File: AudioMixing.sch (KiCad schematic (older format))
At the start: 38 parts, among them U6 MAX98089ETN+, Y2 830208220101

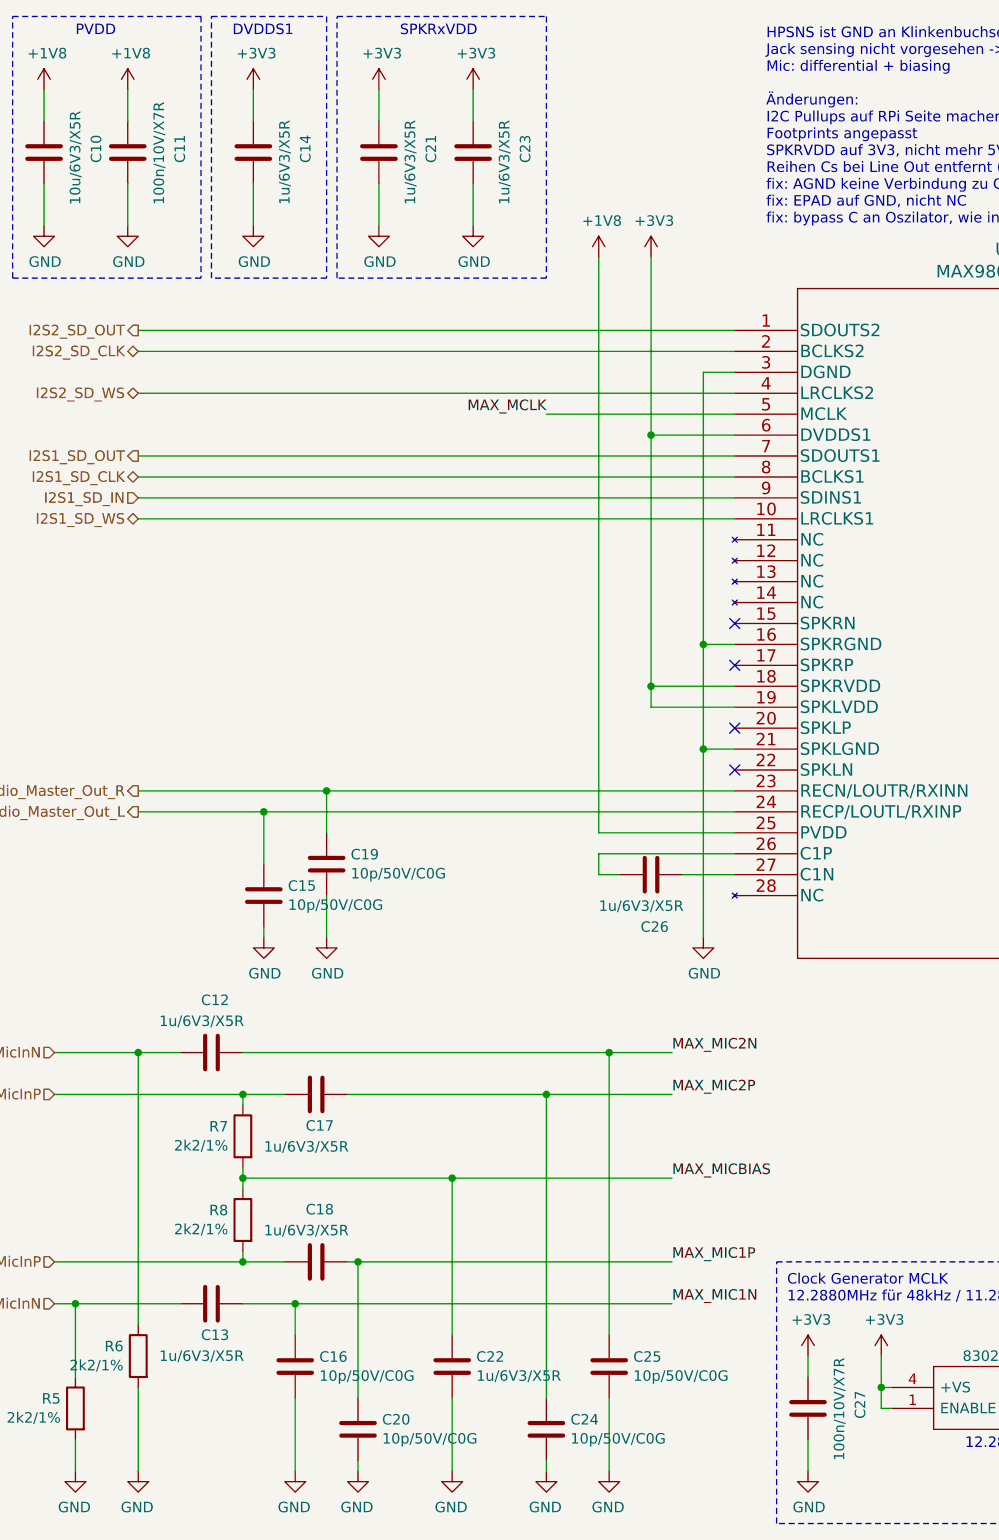
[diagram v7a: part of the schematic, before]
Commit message: - Platzoptimierungen
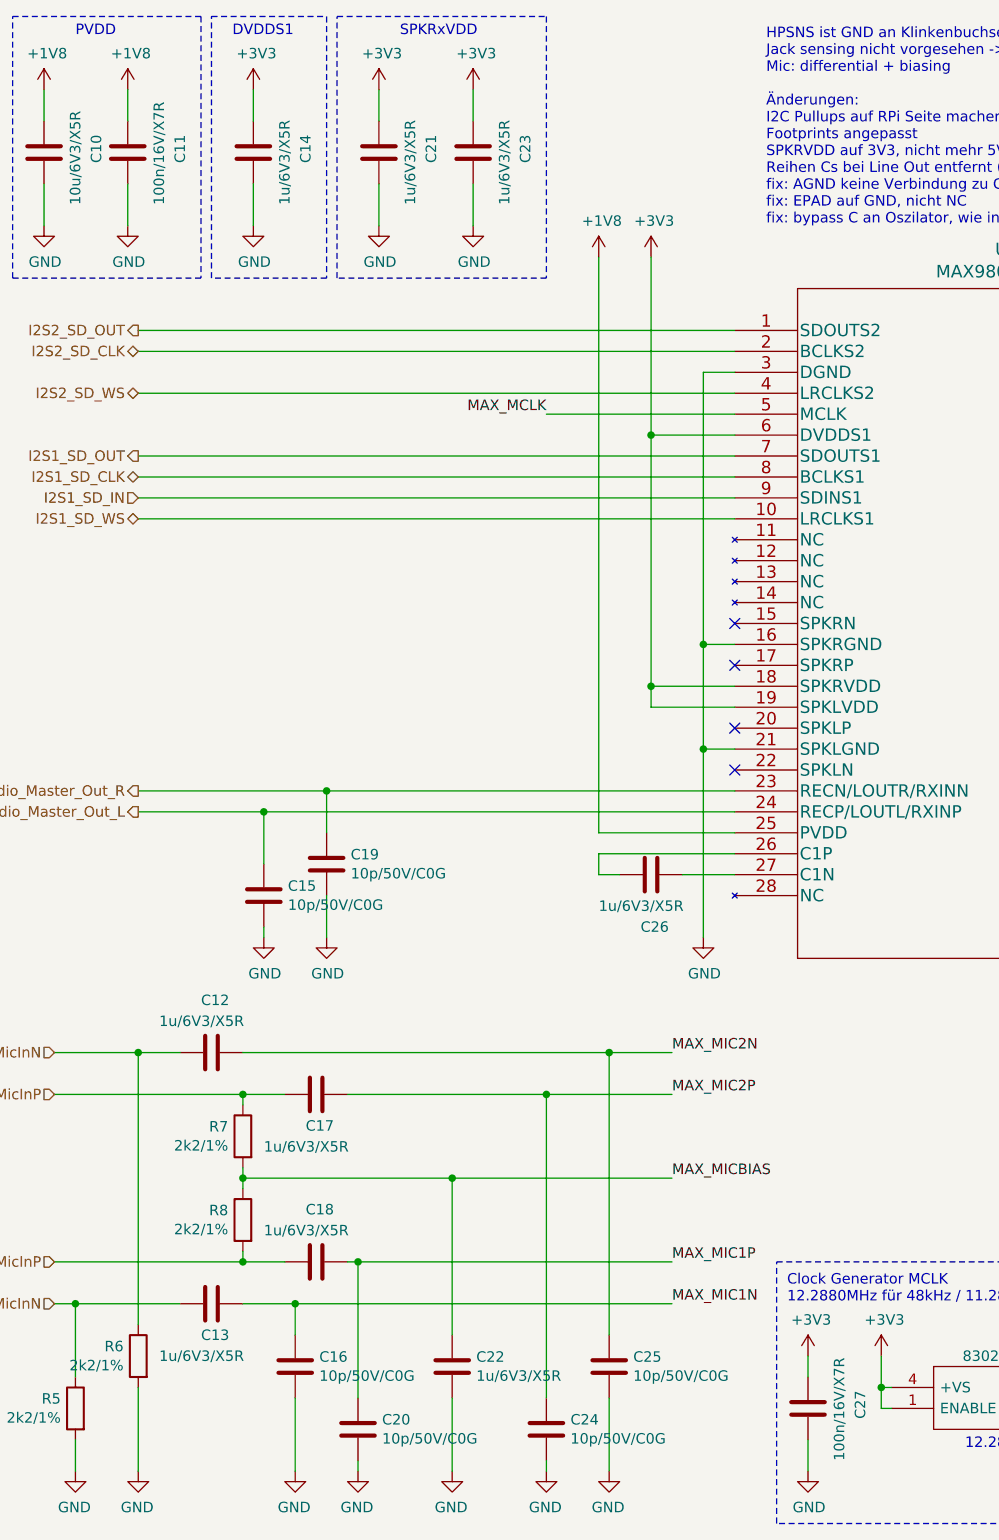
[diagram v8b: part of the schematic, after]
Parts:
- C10, C33: footprint Resistor_SMD:R_0603_1608Metric -> Capacitor_SMD:C_0603_1608Metric
- C11, C27: value 100n/10V/X7R -> 100n/16V/X7R; footprint Resistor_SMD:R_0603_1608Metric -> Capacitor_SMD:C_0402_1005Metric
- C12, C13, C14, C15, C16, C17, C18, C19, C20, C21, C22, C23, C24, C25, C26, C28, C29, C30, C31, C32, C34, C35, C36, C37, C38, C39, C40: footprint Resistor_SMD:R_0603_1608Metric -> Capacitor_SMD:C_0402_1005Metric
- R5, R6, R7, R8, R9: footprint Resistor_SMD:R_0603_1608Metric -> Resistor_SMD:R_0402_1005Metric
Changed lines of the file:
@@
 F 0 "C15" H 2415 4796 50  0000 L CNN
 F 1 "10p/50V/C0G" H 2415 4705 50  0000 L CNN
-F 2 "Resistor_SMD:R_0603_1608Metric" H 2338 4600 50  0001 C CNN
+F 2 "Capacitor_SMD:C_0402_1005Metric" H 2338 4600 50  0001 C CNN
 F 3 "~" H 2300 4750 50  0001 C CNN
 	1    2300 4750
@@
 F 0 "C19" H 2715 4646 50  0000 L CNN
 F 1 "10p/50V/C0G" H 2715 4555 50  0000 L CNN
-F 2 "Resistor_SMD:R_0603_1608Metric" H 2638 4450 50  0001 C CNN
+F 2 "Capacitor_SMD:C_0402_1005Metric" H 2638 4450 50  0001 C CNN
 F 3 "~" H 2600 4600 50  0001 C CNN
 	1    2600 4600
@@
 F 0 "C30" H 8165 5346 50  0000 L CNN
 F 1 "10p/50V/C0G" H 8165 5255 50  0000 L CNN
-F 2 "Resistor_SMD:R_0603_1608Metric" H 8088 5150 50  0001 C CNN
+F 2 "Capacitor_SMD:C_0402_1005Metric" H 8088 5150 50  0001 C CNN
 F 3 "~" H 8050 5300 50  0001 C CNN
 	1    8050 5300
@@
 F 0 "C31" H 8465 4946 50  0000 L CNN
 F 1 "10p/50V/C0G" H 8465 4855 50  0000 L CNN
-F 2 "Resistor_SMD:R_0603_1608Metric" H 8388 4750 50  0001 C CNN
+F 2 "Capacitor_SMD:C_0402_1005Metric" H 8388 4750 50  0001 C CNN
 F 3 "~" H 8350 4900 50  0001 C CNN
 	1    8350 4900
@@
 F 0 "C36" H 9515 4946 50  0000 L CNN
 F 1 "10p/50V/C0G" H 9515 4855 50  0000 L CNN
-F 2 "Resistor_SMD:R_0603_1608Metric" H 9438 4750 50  0001 C CNN
+F 2 "Capacitor_SMD:C_0402_1005Metric" H 9438 4750 50  0001 C CNN
 F 3 "~" H 9400 4900 50  0001 C CNN
 	1    9400 4900
@@
 F 0 "C39" H 9865 5146 50  0000 L CNN
 F 1 "10p/50V/C0G" H 9865 5055 50  0000 L CNN
-F 2 "Resistor_SMD:R_0603_1608Metric" H 9788 4950 50  0001 C CNN
+F 2 "Capacitor_SMD:C_0402_1005Metric" H 9788 4950 50  0001 C CNN
 F 3 "~" H 9750 5100 50  0001 C CNN
 	1    9750 5100
@@
 F 0 "C26" V 4400 4600 50  0000 L CNN
 F 1 "1u/6V3/X5R" V 4300 4400 50  0000 L CNN
-F 2 "Resistor_SMD:R_0603_1608Metric" H 4188 4500 50  0001 C CNN
+F 2 "Capacitor_SMD:C_0402_1005Metric" H 4188 4500 50  0001 C CNN
 F 3 "~" H 4150 4650 50  0001 C CNN
 	1    4150 4650
@@
 F 0 "C29" H 7865 5146 50  0000 L CNN
 F 1 "1u/6V3/X5R" H 7865 5055 50  0000 L CNN
-F 2 "Resistor_SMD:R_0603_1608Metric" H 7788 4950 50  0001 C CNN
+F 2 "Capacitor_SMD:C_0402_1005Metric" H 7788 4950 50  0001 C CNN
 F 3 "~" H 7750 5100 50  0001 C CNN
 	1    7750 5100
@@
 F 0 "C28" H 7565 4946 50  0000 L CNN
 F 1 "1u/6V3/X5R" H 7565 4855 50  0000 L CNN
-F 2 "Resistor_SMD:R_0603_1608Metric" H 7488 4750 50  0001 C CNN
+F 2 "Capacitor_SMD:C_0402_1005Metric" H 7488 4750 50  0001 C CNN
 F 3 "~" H 7450 4900 50  0001 C CNN
 	1    7450 4900
@@
 F 0 "C35" H 9165 5346 50  0000 L CNN
 F 1 "1u/6V3/X5R" H 9165 5255 50  0000 L CNN
-F 2 "Resistor_SMD:R_0603_1608Metric" H 9088 5150 50  0001 C CNN
+F 2 "Capacitor_SMD:C_0402_1005Metric" H 9088 5150 50  0001 C CNN
 F 3 "~" H 9050 5300 50  0001 C CNN
 	1    9050 5300
@@
 F 0 "C33" H 8815 5146 50  0000 L CNN
 F 1 "2u2/6V3/X5R" H 8815 5055 50  0000 L CNN
-F 2 "Resistor_SMD:R_0603_1608Metric" H 8738 4950 50  0001 C CNN
+F 2 "Capacitor_SMD:C_0603_1608Metric" H 8738 4950 50  0001 C CNN
 F 3 "~" H 8700 5100 50  0001 C CNN
 	1    8700 5100
@@
 F 0 "C38" V 9900 3900 50  0000 L CNN
 F 1 "1u/6V3/X5R" V 9800 3700 50  0000 L CNN
-F 2 "Resistor_SMD:R_0603_1608Metric" H 9688 3800 50  0001 C CNN
+F 2 "Capacitor_SMD:C_0402_1005Metric" H 9688 3800 50  0001 C CNN
 F 3 "~" H 9650 3950 50  0001 C CNN
 	1    9650 3950
@@
 F 0 "C40" V 9800 4050 50  0000 L CNN
 F 1 "1u/6V3/X5R" V 9700 3850 50  0000 L CNN
-F 2 "Resistor_SMD:R_0603_1608Metric" H 9988 3950 50  0001 C CNN
+F 2 "Capacitor_SMD:C_0402_1005Metric" H 9988 3950 50  0001 C CNN
 F 3 "~" H 9950 4100 50  0001 C CNN
 	1    9950 4100
@@
 F 0 "R9" H 7970 1946 50  0000 L CNN
 F 1 "10k/5%" H 7970 1855 50  0000 L CNN
-F 2 "Resistor_SMD:R_0603_1608Metric" V 7830 1900 50  0001 C CNN
+F 2 "Resistor_SMD:R_0402_1005Metric" V 7830 1900 50  0001 C CNN
 F 3 "~" H 7900 1900 50  0001 C CNN
 	1    7900 1900
@@
 F 0 "C32" V 8700 1150 50  0000 L CNN
 F 1 "1u/6V3/X5R" V 8600 950 50  0000 L CNN
-F 2 "Resistor_SMD:R_0603_1608Metric" H 8488 1050 50  0001 C CNN
+F 2 "Capacitor_SMD:C_0402_1005Metric" H 8488 1050 50  0001 C CNN
 F 3 "~" H 8450 1200 50  0001 C CNN
 	1    8450 1200
@@
 F 0 "C34" V 9100 1150 50  0000 L CNN
 F 1 "1u/6V3/X5R" V 9000 950 50  0000 L CNN
-F 2 "Resistor_SMD:R_0603_1608Metric" H 8888 1050 50  0001 C CNN
+F 2 "Capacitor_SMD:C_0402_1005Metric" H 8888 1050 50  0001 C CNN
 F 3 "~" H 8850 1200 50  0001 C CNN
 	1    8850 1200
@@
 F 0 "C37" V 9700 1150 50  0000 L CNN
 F 1 "1u/6V3/X5R" V 9600 950 50  0000 L CNN
-F 2 "Resistor_SMD:R_0603_1608Metric" H 9488 1050 50  0001 C CNN
+F 2 "Capacitor_SMD:C_0402_1005Metric" H 9488 1050 50  0001 C CNN
 F 3 "~" H 9450 1200 50  0001 C CNN
 	1    9450 1200
@@
 F 0 "C23" V 3550 1150 50  0000 L CNN
 F 1 "1u/6V3/X5R" V 3450 950 50  0000 L CNN
-F 2 "Resistor_SMD:R_0603_1608Metric" H 3338 1050 50  0001 C CNN
+F 2 "Capacitor_SMD:C_0402_1005Metric" H 3338 1050 50  0001 C CNN
 F 3 "~" H 3300 1200 50  0001 C CNN
 	1    3300 1200
@@
 F 0 "C14" V 2500 1150 50  0000 L CNN
 F 1 "1u/6V3/X5R" V 2400 950 50  0000 L CNN
-F 2 "Resistor_SMD:R_0603_1608Metric" H 2288 1050 50  0001 C CNN
+F 2 "Capacitor_SMD:C_0402_1005Metric" H 2288 1050 50  0001 C CNN
 F 3 "~" H 2250 1200 50  0001 C CNN
 	1    2250 1200
@@
 F 0 "C21" V 3100 1150 50  0000 L CNN
 F 1 "1u/6V3/X5R" V 3000 950 50  0000 L CNN
-F 2 "Resistor_SMD:R_0603_1608Metric" H 2888 1050 50  0001 C CNN
+F 2 "Capacitor_SMD:C_0402_1005Metric" H 2888 1050 50  0001 C CNN
 F 3 "~" H 2850 1200 50  0001 C CNN
 	1    2850 1200
@@
 F 0 "C10" V 1500 1150 50  0000 L CNN
 F 1 "10u/6V3/X5R" V 1400 950 50  0000 L CNN
-F 2 "Resistor_SMD:R_0603_1608Metric" H 1288 1050 50  0001 C CNN
+F 2 "Capacitor_SMD:C_0603_1608Metric" H 1288 1050 50  0001 C CNN
 F 3 "~" H 1250 1200 50  0001 C CNN
 	1    1250 1200
@@
 P 1650 1200
 F 0 "C11" V 1900 1150 50  0000 L CNN
-F 1 "100n/10V/X7R" V 1800 950 50  0000 L CNN
-F 2 "Resistor_SMD:R_0603_1608Metric" H 1688 1050 50  0001 C CNN
+F 1 "100n/16V/X7R" V 1800 950 50  0000 L CNN
+F 2 "Capacitor_SMD:C_0402_1005Metric" H 1688 1050 50  0001 C CNN
 F 3 "~" H 1650 1200 50  0001 C CNN
 	1    1650 1200
@@
 F 0 "C17" V 2400 5650 50  0000 L CNN
 F 1 "1u/6V3/X5R" V 2300 5450 50  0000 L CNN
-F 2 "Resistor_SMD:R_0603_1608Metric" H 2588 5550 50  0001 C CNN
+F 2 "Capacitor_SMD:C_0402_1005Metric" H 2588 5550 50  0001 C CNN
 F 3 "~" H 2550 5700 50  0001 C CNN
 	1    2550 5700
@@
 F 0 "C18" V 2800 6450 50  0000 L CNN
 F 1 "1u/6V3/X5R" V 2700 6250 50  0000 L CNN
-F 2 "Resistor_SMD:R_0603_1608Metric" H 2588 6350 50  0001 C CNN
+F 2 "Capacitor_SMD:C_0402_1005Metric" H 2588 6350 50  0001 C CNN
 F 3 "~" H 2550 6500 50  0001 C CNN
 	1    2550 6500
@@
 F 0 "C13" V 1900 6650 50  0000 L CNN
 F 1 "1u/6V3/X5R" V 1800 6450 50  0000 L CNN
-F 2 "Resistor_SMD:R_0603_1608Metric" H 2088 6550 50  0001 C CNN
+F 2 "Capacitor_SMD:C_0402_1005Metric" H 2088 6550 50  0001 C CNN
 F 3 "~" H 2050 6700 50  0001 C CNN
 	1    2050 6700
@@
 F 0 "C12" V 2300 5450 50  0000 L CNN
 F 1 "1u/6V3/X5R" V 2200 5250 50  0000 L CNN
-F 2 "Resistor_SMD:R_0603_1608Metric" H 2088 5350 50  0001 C CNN
+F 2 "Capacitor_SMD:C_0402_1005Metric" H 2088 5350 50  0001 C CNN
 F 3 "~" H 2050 5500 50  0001 C CNN
 	1    2050 5500
@@
 F 0 "R8" H 2270 6346 50  0000 L CNN
 F 1 "2k2/1%" H 2270 6255 50  0000 L CNN
-F 2 "Resistor_SMD:R_0603_1608Metric" V 2130 6300 50  0001 C CNN
+F 2 "Resistor_SMD:R_0402_1005Metric" V 2130 6300 50  0001 C CNN
 F 3 "~" H 2200 6300 50  0001 C CNN
 	1    2200 6300
@@
 F 0 "R7" H 2270 5946 50  0000 L CNN
 F 1 "2k2/1%" H 2270 5855 50  0000 L CNN
-F 2 "Resistor_SMD:R_0603_1608Metric" V 2130 5900 50  0001 C CNN
+F 2 "Resistor_SMD:R_0402_1005Metric" V 2130 5900 50  0001 C CNN
 F 3 "~" H 2200 5900 50  0001 C CNN
 	1    2200 5900
@@
 F 0 "R5" H 1470 7246 50  0000 L CNN
 F 1 "2k2/1%" H 1470 7155 50  0000 L CNN
-F 2 "Resistor_SMD:R_0603_1608Metric" V 1330 7200 50  0001 C CNN
+F 2 "Resistor_SMD:R_0402_1005Metric" V 1330 7200 50  0001 C CNN
 F 3 "~" H 1400 7200 50  0001 C CNN
 	1    1400 7200
@@
 F 0 "R6" H 1770 6996 50  0000 L CNN
 F 1 "2k2/1%" H 1770 6905 50  0000 L CNN
-F 2 "Resistor_SMD:R_0603_1608Metric" V 1630 6950 50  0001 C CNN
+F 2 "Resistor_SMD:R_0402_1005Metric" V 1630 6950 50  0001 C CNN
 F 3 "~" H 1700 6950 50  0001 C CNN
 	1    1700 6950
@@
 F 0 "C20" H 2865 7346 50  0000 L CNN
 F 1 "10p/50V/C0G" H 2865 7255 50  0000 L CNN
-F 2 "Resistor_SMD:R_0603_1608Metric" H 2788 7150 50  0001 C CNN
+F 2 "Capacitor_SMD:C_0402_1005Metric" H 2788 7150 50  0001 C CNN
 F 3 "~" H 2750 7300 50  0001 C CNN
 	1    2750 7300
@@
 F 0 "C16" H 2565 7046 50  0000 L CNN
 F 1 "10p/50V/C0G" H 2565 6955 50  0000 L CNN
-F 2 "Resistor_SMD:R_0603_1608Metric" H 2488 6850 50  0001 C CNN
+F 2 "Capacitor_SMD:C_0402_1005Metric" H 2488 6850 50  0001 C CNN
 F 3 "~" H 2450 7000 50  0001 C CNN
 	1    2450 7000
@@
 F 0 "C24" H 3765 7346 50  0000 L CNN
 F 1 "10p/50V/C0G" H 3765 7255 50  0000 L CNN
-F 2 "Resistor_SMD:R_0603_1608Metric" H 3688 7150 50  0001 C CNN
+F 2 "Capacitor_SMD:C_0402_1005Metric" H 3688 7150 50  0001 C CNN
 F 3 "~" H 3650 7300 50  0001 C CNN
 	1    3650 7300
@@
 F 0 "C25" H 4065 7046 50  0000 L CNN
 F 1 "10p/50V/C0G" H 4065 6955 50  0000 L CNN
-F 2 "Resistor_SMD:R_0603_1608Metric" H 3988 6850 50  0001 C CNN
+F 2 "Capacitor_SMD:C_0402_1005Metric" H 3988 6850 50  0001 C CNN
 F 3 "~" H 3950 7000 50  0001 C CNN
 	1    3950 7000
@@
 F 0 "C22" H 3315 7046 50  0000 L CNN
 F 1 "1u/6V3/X5R" H 3315 6955 50  0000 L CNN
-F 2 "Resistor_SMD:R_0603_1608Metric" H 3238 6850 50  0001 C CNN
+F 2 "Capacitor_SMD:C_0402_1005Metric" H 3238 6850 50  0001 C CNN
 F 3 "~" H 3200 7000 50  0001 C CNN
 	1    3200 7000
@@
 P 4900 7200
 F 0 "C27" V 5150 7150 50  0000 L CNN
-F 1 "100n/10V/X7R" V 5050 6950 50  0000 L CNN
-F 2 "Resistor_SMD:R_0603_1608Metric" H 4938 7050 50  0001 C CNN
+F 1 "100n/16V/X7R" V 5050 6950 50  0000 L CNN
+F 2 "Capacitor_SMD:C_0402_1005Metric" H 4938 7050 50  0001 C CNN
 F 3 "~" H 4900 7200 50  0001 C CNN
 	1    4900 7200
